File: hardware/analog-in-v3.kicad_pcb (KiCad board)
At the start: 2 copper layers, 30 x 35 mm, 37 parts, among them P1 CON-SENSOR2, P2 CONN_5, P3 BOOT, P4 DEBUG, U1 XMC110024, U2 TLV272IS, U3 DRILL, U4 DRILL, U5 DRILL, U6 DRILL

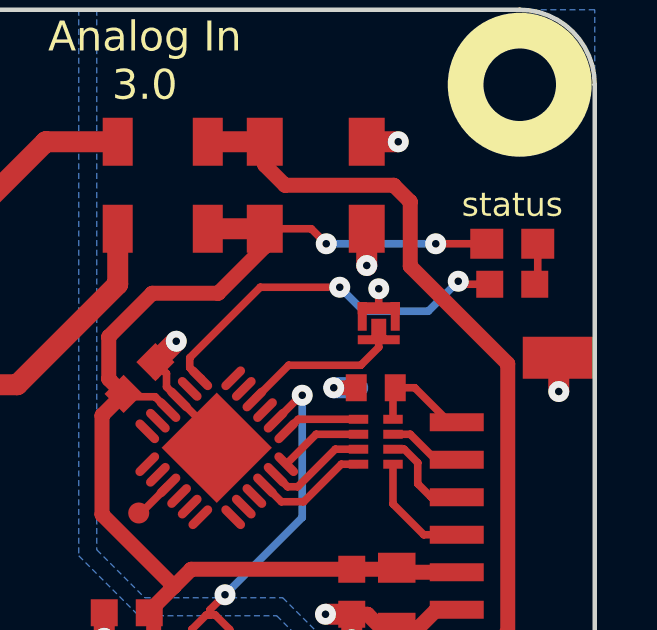
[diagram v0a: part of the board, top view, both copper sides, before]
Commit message: Change capacitor footprint(s) to C0402F
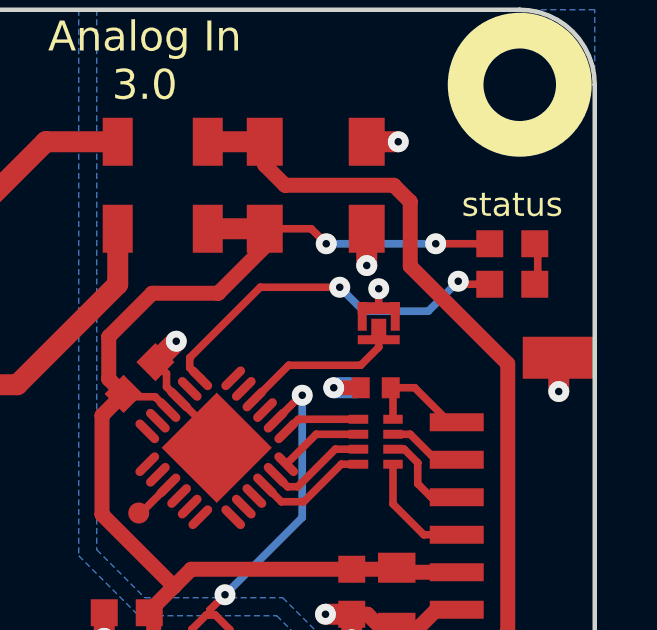
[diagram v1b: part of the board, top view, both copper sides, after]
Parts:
- C5: footprint kicad-libraries:C0402E -> kicad-libraries:C0402F
- D3: footprint kicad-libraries:D0603E -> kicad-libraries:D0603F
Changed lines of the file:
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@@
-(kicad_pcb (version 4) (host pcbnew 4.0.7-e2-6376~58~ubuntu17.04.1)
+(kicad_pcb (version 4) (host pcbnew 4.0.2+dfsg1-stable)
   (general
     (links 65)
     (no_connects 0)
-    (area 174.644999 93.744999 282.39286 160.39)
+    (area 175.424999 94.524999 205.575001 129.675001)
     (thickness 1.6)
     (drawings 21)
@@
     )
   )
-  (module kicad-libraries:C0402E (layer F.Cu)
-    (at 198.2 107.2 180)
-    (attr smd)
-    (fp_text reference C5 (at 0 0.125 180) (layer F.Fab)
-      (effects (font (size 0.2 0.2) (thickness 0.05)))
-    )
-    (fp_text value 220pF (at 0 -0.275 180) (layer F.Fab)
-      (effects (font (size 0.2 0.2) (thickness 0.05)))
-    )
-    (fp_line (start -0.8509 -0.44958) (end 0.8509 -0.44958) (layer F.Fab) (width 0.001))
-    (fp_line (start 0.8509 -0.44958) (end 0.8509 0.44958) (layer F.Fab) (width 0.001))
-    (fp_line (start 0.8509 0.44958) (end -0.8509 0.44958) (layer F.Fab) (width 0.001))
-    (fp_line (start -0.8509 0.44958) (end -0.8509 -0.44958) (layer F.Fab) (width 0.001))
-    (pad 1 smd rect (at -0.65 0 180) (size 0.7 0.9) (layers F.Cu F.Paste F.Mask)
-      (net 16 "Net-(C5-Pad1)"))
-    (pad 2 smd rect (at 0.65 0 180) (size 0.7 0.9) (layers F.Cu F.Paste F.Mask)
-      (net 2 GND))
-    (model Capacitors_SMD/C_0402.wrl
-      (at (xyz 0 0 0))
-      (scale (xyz 1 1 1))
-      (rotate (xyz 0 0 0))
-    )
-  )
   (module kicad-libraries:C0603F (layer F.Cu)
     (at 197.4 114 270)
@@
     )
   )
-  (module kicad-libraries:D0603E (layer F.Cu)
-    (at 202.75 102.4)
-    (attr smd)
-    (fp_text reference D3 (at 0.85 0.45) (layer F.Fab)
-      (effects (font (size 0.2 0.2) (thickness 0.05)))
-    )
-    (fp_text value blue (at 0.85 -0.5) (layer F.Fab)
-      (effects (font (size 0.2 0.2) (thickness 0.05)))
-    )
-    (fp_line (start 0.2 -0.4) (end 0.2 0.4) (layer F.Fab) (width 0.05))
-    (fp_line (start 0.2 0) (end -0.2 -0.4) (layer F.Fab) (width 0.05))
-    (fp_line (start -0.2 -0.4) (end -0.2 0.4) (layer F.Fab) (width 0.05))
-    (fp_line (start -0.2 0.4) (end 0.2 0) (layer F.Fab) (width 0.05))
-    (fp_line (start -0.889 -0.254) (end -0.889 0.254) (layer F.Fab) (width 0.05))
-    (fp_line (start -1.143 0) (end -0.635 0) (layer F.Fab) (width 0.05))
-    (fp_line (start -1.45034 -0.65024) (end 1.45034 -0.65024) (layer F.Fab) (width 0.001))
-    (fp_line (start 1.45034 -0.65024) (end 1.45034 0.65024) (layer F.Fab) (width 0.001))
-    (fp_line (start 1.45034 0.65024) (end -1.45034 0.65024) (layer F.Fab) (width 0.001))
-    (fp_line (start -1.45034 0.65024) (end -1.45034 -0.65024) (layer F.Fab) (width 0.001))
-    (pad 1 smd rect (at -0.8501 0) (size 1.1 1) (layers F.Cu F.Paste F.Mask)
-      (net 1 3V3))
-    (pad 2 smd rect (at 0.8501 0) (size 1.1 1) (layers F.Cu F.Paste F.Mask)
-      (net 17 "Net-(D3-Pad2)"))
-    (model LED_SMD/D_0603_blue.wrl
-      (at (xyz 0 0 0))
-      (scale (xyz 1 1 1))
-      (rotate (xyz 90 180 0))
-    )
-  )
   (module kicad-libraries:SolderJumper (layer F.Cu)
     (at 198.3 105.05 270)
@@
     )
   )
+  (module kicad-libraries:C0402F (layer F.Cu)
+    (at 198.2 107.2 180)
+    (fp_text reference C5 (at 0.1 0.15 180) (layer F.Fab)
+      (effects (font (size 0.2 0.2) (thickness 0.05)))
+    )
+    (fp_text value 220pF (at 0 -0.15 180) (layer F.Fab)
+      (effects (font (size 0.2 0.2) (thickness 0.05)))
+    )
+    (fp_line (start -0.9 -0.45) (end 0.9 -0.45) (layer F.Fab) (width 0.025))
+    (fp_line (start 0.9 -0.45) (end 0.9 0.45) (layer F.Fab) (width 0.025))
+    (fp_line (start 0.9 0.45) (end -0.9 0.45) (layer F.Fab) (width 0.025))
+    (fp_line (start -0.9 0.45) (end -0.9 -0.45) (layer F.Fab) (width 0.025))
+    (pad 2 smd rect (at 0.5 0 180) (size 0.6 0.7) (layers F.Cu F.Paste F.Mask)
+      (net 2 GND))
+    (pad 1 smd rect (at -0.5 0 180) (size 0.6 0.7) (layers F.Cu F.Paste F.Mask)
+      (net 16 "Net-(C5-Pad1)"))
+    (model Capacitors_SMD/C_0402.wrl
+      (at (xyz 0 0 0))
+      (scale (xyz 1 1 1))
+      (rotate (xyz 0 0 0))
+    )
+  )
+  (module kicad-libraries:D0603F (layer F.Cu)
+    (at 202.75 102.4)
+    (attr smd)
+    (fp_text reference D3 (at -0.775 0.45) (layer F.Fab)
+      (effects (font (size 0.2 0.2) (thickness 0.05)))
+    )
+    (fp_text value blue (at 0.75 0.45) (layer F.Fab)
+      (effects (font (size 0.2 0.2) (thickness 0.05)))
+    )
+    (fp_line (start -0.75 -0.3) (end -0.75 0.3) (layer F.Fab) (width 0.05))
+    (fp_line (start -1.05 0) (end -0.45 0) (layer F.Fab) (width 0.05))
+    (fp_line (start 0.45 0) (end 1.05 0) (layer F.Fab) (width 0.05))
+    (fp_line (start 0 -0.3) (end 0 0.3) (layer F.Fab) (width 0.05))
+    (fp_line (start -0.3 -0.3) (end -0.3 0.3) (layer F.Fab) (width 0.05))
+    (fp_line (start -0.3 0.3) (end 0 0) (layer F.Fab) (width 0.05))
+    (fp_line (start 0 0) (end -0.3 -0.3) (layer F.Fab) (width 0.05))
+    (fp_line (start -1.45034 -0.65024) (end 1.45034 -0.65024) (layer F.Fab) (width 0.001))
+    (fp_line (start 1.45034 -0.65024) (end 1.45034 0.65024) (layer F.Fab) (width 0.001))
+    (fp_line (start 1.45034 0.65024) (end -1.45034 0.65024) (layer F.Fab) (width 0.001))
+    (fp_line (start -1.45034 0.65024) (end -1.45034 -0.65024) (layer F.Fab) (width 0.001))
+    (pad 1 smd rect (at -0.75 0) (size 0.9 0.9) (layers F.Cu F.Paste F.Mask)
+      (net 1 3V3))
+    (pad 2 smd rect (at 0.75 0) (size 0.9 0.9) (layers F.Cu F.Paste F.Mask)
+      (net 17 "Net-(D3-Pad2)"))
+    (model LED_SMD/D_0603_blue.wrl
+      (at (xyz 0 0 0))
+      (scale (xyz 1 1 1))
+      (rotate (xyz -90 0 0))
+    )
+  )
